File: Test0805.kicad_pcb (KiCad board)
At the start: 2 copper layers, 0 parts

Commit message: Position footprints.
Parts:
- added BT1: 9V, footprints:BatteryHolder_Keystone_968_1x9V, F.Cu at (134.6, 109.2)
- added D1: LED, LEDs:LED_0805, F.Cu at (136.5, 104.8)
- added D2: LED, LEDs:LED_0805, F.Cu at (136.5, 113.7)
- added D3: LED, LEDs:LED_0805, F.Cu at (145.4, 104.8)
- added D4: LED, LEDs:LED_0805, F.Cu at (145.4, 113.7)
- added R1: R, Resistors_SMD:R_0805, F.Cu at (141.0, 108.0)
- added R2: R, Resistors_SMD:R_0805, F.Cu at (141.0, 110.5)

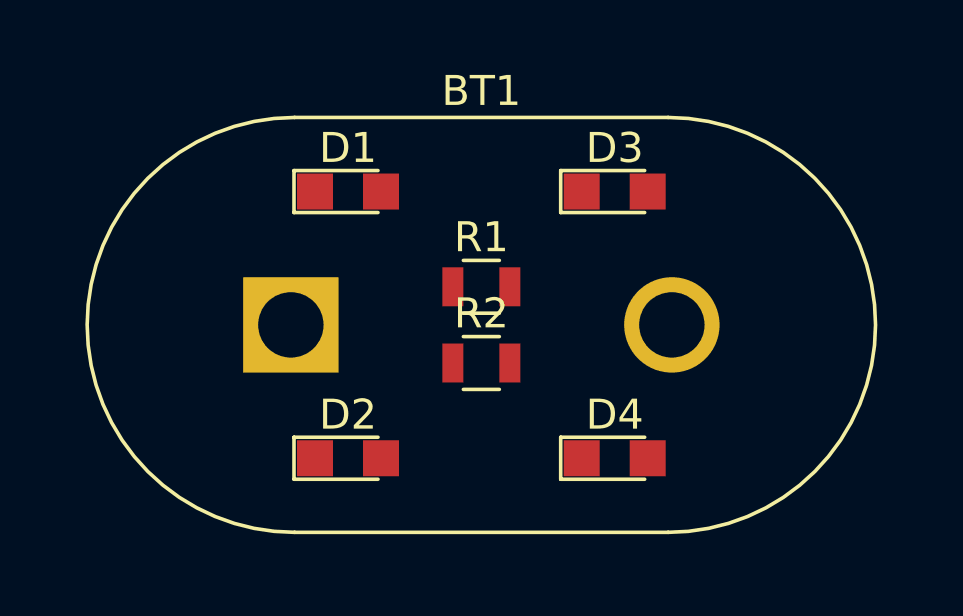
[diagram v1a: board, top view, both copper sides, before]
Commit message: Make references invisible.
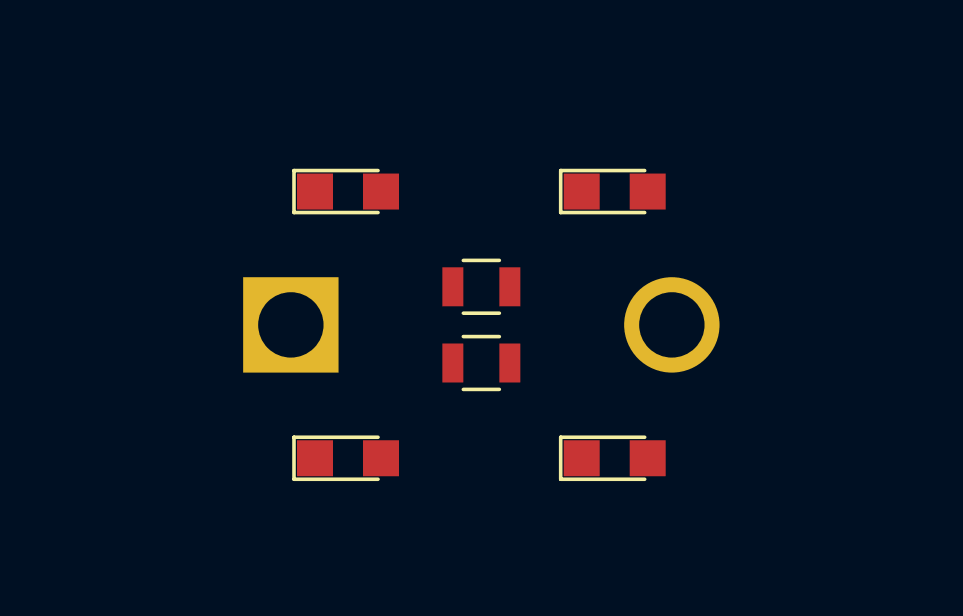
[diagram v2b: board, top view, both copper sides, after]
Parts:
- BT1: moved to B.Cu
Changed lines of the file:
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@@
     (46 B.CrtYd user)
     (47 F.CrtYd user)
-    (48 B.Fab user)
+    (48 B.Fab user hide)
     (49 F.Fab user hide)
   )
@@
     (add_net "Net-(D2-Pad2)")
   )
-  (module footprints:BatteryHolder_Keystone_968_1x9V (layer F.Cu)
+  (module footprints:BatteryHolder_Keystone_968_1x9V (layer B.Cu)
     (at 134.62 109.22)
     (descr "9V battery snap, http://www.keyelco.com/product-pdf.cfm?p=1072")
     (tags "9V battery snap")
-    (fp_text reference BT1 (at 6.35 -7.795) (layer F.SilkS)
-      (effects (font (size 1 1) (thickness 0.15)))
-    )
-    (fp_text value 9V (at 6.35 7.795) (layer F.Fab)
-      (effects (font (size 1 1) (thickness 0.15)))
-    )
-    (fp_arc (start 0.125 0) (end 0.125 6.795) (angle 180) (layer F.Fab) (width 0.1))
-    (fp_arc (start 12.575 0) (end 12.575 -6.795) (angle 180) (layer F.Fab) (width 0.1))
-    (fp_arc (start 0.125 0) (end 0.125 6.915) (angle 180) (layer F.SilkS) (width 0.12))
-    (fp_arc (start 12.575 0) (end 12.575 -6.915) (angle 180) (layer F.SilkS) (width 0.12))
-    (fp_line (start 0.125 -6.795) (end 12.575 -6.795) (layer F.Fab) (width 0.1))
-    (fp_line (start 0.125 6.795) (end 12.575 6.795) (layer F.Fab) (width 0.1))
-    (fp_line (start 0.125 -6.915) (end 12.575 -6.915) (layer F.SilkS) (width 0.12))
-    (fp_line (start 0.125 6.915) (end 12.575 6.915) (layer F.SilkS) (width 0.12))
-    (fp_line (start -7.17 -7.295) (end -7.17 7.295) (layer F.CrtYd) (width 0.05))
-    (fp_line (start -7.17 7.295) (end 19.87 7.295) (layer F.CrtYd) (width 0.05))
-    (fp_line (start 19.87 7.295) (end 19.87 -7.295) (layer F.CrtYd) (width 0.05))
-    (fp_line (start 19.87 -7.295) (end -7.17 -7.295) (layer F.CrtYd) (width 0.05))
-    (fp_text user %R (at 6.35 0) (layer F.Fab)
-      (effects (font (size 1 1) (thickness 0.15)))
+    (fp_text reference BT1 (at 6.35 7.795) (layer B.SilkS) hide
+      (effects (font (size 1 1) (thickness 0.15)) (justify mirror))
+    )
+    (fp_text value 9V (at 6.35 -7.795) (layer B.Fab)
+      (effects (font (size 1 1) (thickness 0.15)) (justify mirror))
+    )
+    (fp_arc (start 0.125 0) (end 0.125 -6.795) (angle -180) (layer B.Fab) (width 0.1))
+    (fp_arc (start 12.575 0) (end 12.575 6.795) (angle -180) (layer B.Fab) (width 0.1))
+    (fp_arc (start 0.125 0) (end 0.125 -6.915) (angle -180) (layer B.SilkS) (width 0.12))
+    (fp_arc (start 12.575 0) (end 12.575 6.915) (angle -180) (layer B.SilkS) (width 0.12))
+    (fp_line (start 0.125 6.795) (end 12.575 6.795) (layer B.Fab) (width 0.1))
+    (fp_line (start 0.125 -6.795) (end 12.575 -6.795) (layer B.Fab) (width 0.1))
+    (fp_line (start 0.125 6.915) (end 12.575 6.915) (layer B.SilkS) (width 0.12))
+    (fp_line (start 0.125 -6.915) (end 12.575 -6.915) (layer B.SilkS) (width 0.12))
+    (fp_line (start -7.17 7.295) (end -7.17 -7.295) (layer B.CrtYd) (width 0.05))
+    (fp_line (start -7.17 -7.295) (end 19.87 -7.295) (layer B.CrtYd) (width 0.05))
+    (fp_line (start 19.87 -7.295) (end 19.87 7.295) (layer B.CrtYd) (width 0.05))
+    (fp_line (start 19.87 7.295) (end -7.17 7.295) (layer B.CrtYd) (width 0.05))
+    (fp_text user %R (at 6.35 0) (layer B.Fab)
+      (effects (font (size 1 1) (thickness 0.15)) (justify mirror))
     )
     (pad 1 thru_hole rect (at 0 0) (size 3.18 3.18) (drill 2.18) (layers *.Cu *.Mask)
@@
     (tags "LED led 0805 SMD smd SMT smt smdled SMDLED smtled SMTLED")
     (attr smd)
-    (fp_text reference D1 (at 0 -1.45) (layer F.SilkS)
+    (fp_text reference D1 (at 0 -1.45) (layer F.SilkS) hide
       (effects (font (size 1 1) (thickness 0.15)))
     )
@@
     (tags "LED led 0805 SMD smd SMT smt smdled SMDLED smtled SMTLED")
     (attr smd)
-    (fp_text reference D2 (at 0 -1.45) (layer F.SilkS)
+    (fp_text reference D2 (at 0 -1.45) (layer F.SilkS) hide
       (effects (font (size 1 1) (thickness 0.15)))
     )
@@
     (tags "LED led 0805 SMD smd SMT smt smdled SMDLED smtled SMTLED")
     (attr smd)
-    (fp_text reference D3 (at 0 -1.45) (layer F.SilkS)
+    (fp_text reference D3 (at 0 -1.45) (layer F.SilkS) hide
       (effects (font (size 1 1) (thickness 0.15)))
     )
@@
     (tags "LED led 0805 SMD smd SMT smt smdled SMDLED smtled SMTLED")
     (attr smd)
-    (fp_text reference D4 (at 0 -1.45) (layer F.SilkS)
+    (fp_text reference D4 (at 0 -1.45) (layer F.SilkS) hide
       (effects (font (size 1 1) (thickness 0.15)))
     )
@@
     (tags "resistor 0805")
     (attr smd)
-    (fp_text reference R1 (at 0 -1.65) (layer F.SilkS)
+    (fp_text reference R1 (at 0 -1.65) (layer F.SilkS) hide
       (effects (font (size 1 1) (thickness 0.15)))
     )
@@
     (tags "resistor 0805")
     (attr smd)
-    (fp_text reference R2 (at 0 -1.65) (layer F.SilkS)
-      (effects (font (size 1 1) (thickness 0.15)))
-    )
+    (fp_text reference R2 (at 0 -1.65) (layer F.SilkS) hide
+      (effects (font (size 1 1) (thickness 0.15)))
+    )

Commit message: Add board outline.
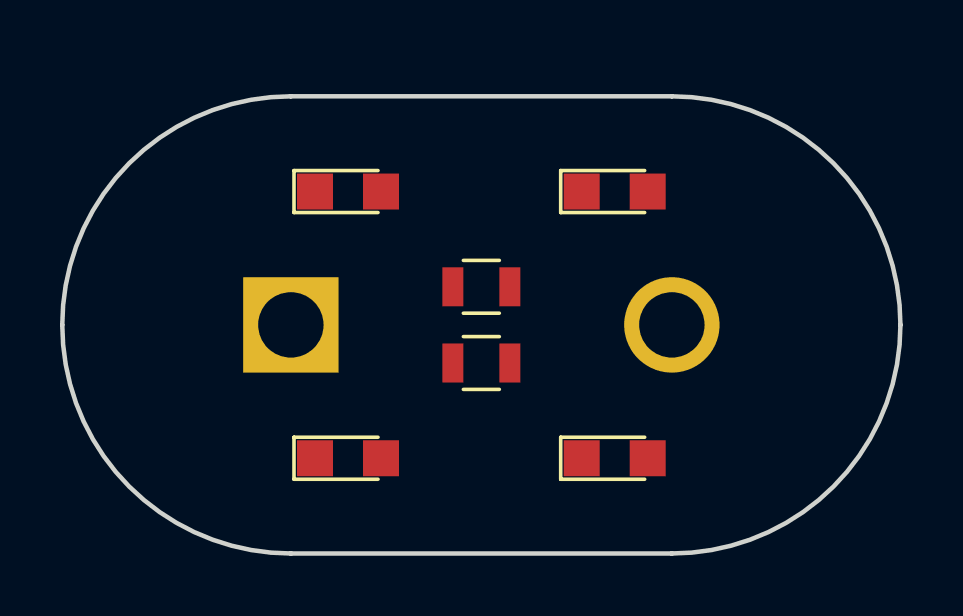
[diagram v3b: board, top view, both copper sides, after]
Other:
- board outline added: 27.9 x 15.2 mm
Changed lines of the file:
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@@
     (area 0 0 0 0)
     (thickness 1.6)
-    (drawings 0)
+    (drawings 6)
     (tracks 0)
     (zones 0)
@@
     )
   )
+  (gr_arc (start 147.32 109.22) (end 147.32 101.6) (angle 90) (layer Edge.Cuts) (width 0.15))
+  (gr_arc (start 147.32 109.22) (end 154.94 109.22) (angle 90) (layer Edge.Cuts) (width 0.15))
+  (gr_arc (start 134.62 109.22) (end 134.62 116.84) (angle 90) (layer Edge.Cuts) (width 0.15))
+  (gr_arc (start 134.62 109.22) (end 127 109.22) (angle 90) (layer Edge.Cuts) (width 0.15))
+  (gr_line (start 134.62 116.84) (end 147.32 116.84) (angle 90) (layer Edge.Cuts) (width 0.15))
+  (gr_line (start 134.62 101.6) (end 147.32 101.6) (angle 90) (layer Edge.Cuts) (width 0.15))
 )

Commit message: Add ground zones.
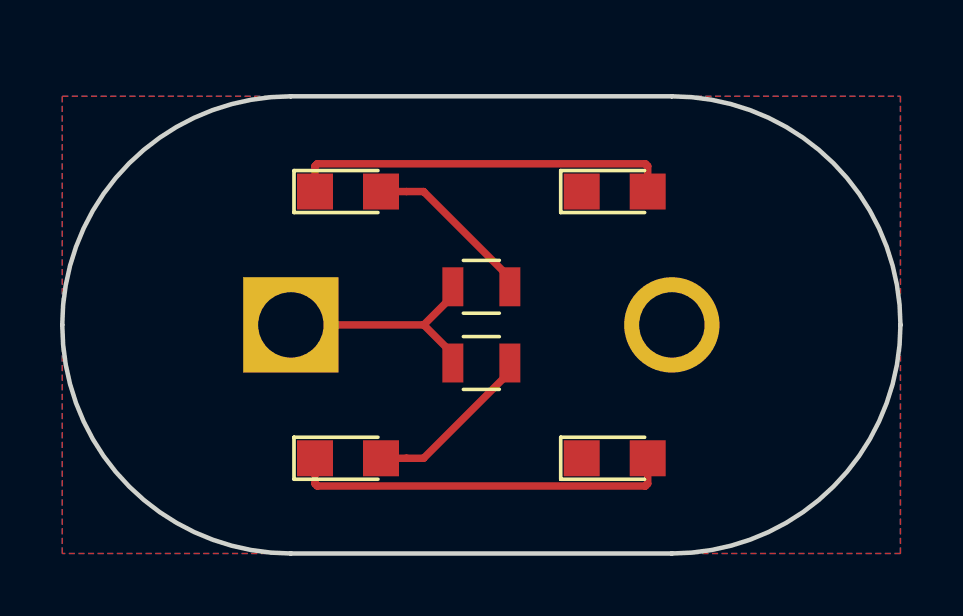
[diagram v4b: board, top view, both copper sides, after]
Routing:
- net Net-(D1-Pad1): track 0.00 -> 12.9 mm
- net Net-(D2-Pad1): track 0.00 -> 12.9 mm
- net Net-(BT1-Pad1): track 0.00 -> 7.77 mm
- net Net-(D2-Pad2): track 0.00 -> 5.79 mm
- net Net-(D1-Pad2): track 0.00 -> 5.79 mm
- added copper zone on B.Cu, net GND
- added copper zone on F.Cu, net GND
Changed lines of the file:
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@@
   (general
     (links 8)
-    (no_connects 8)
+    (no_connects 2)
     (area 0 0 0 0)
     (thickness 1.6)
     (drawings 6)
-    (tracks 0)
+    (tracks 23)
     (zones 0)
     (modules 7)
@@
     (44 Edge.Cuts user)
     (45 Margin user)
-    (46 B.CrtYd user)
+    (46 B.CrtYd user hide)
     (47 F.CrtYd user)
     (48 B.Fab user hide)
@@
     (last_trace_width 0.25)
     (trace_clearance 0.2)
-    (zone_clearance 0.508)
+    (zone_clearance 0.3048)
     (zone_45_only no)
     (trace_min 0.2)
@@
   (gr_line (start 134.62 116.84) (end 147.32 116.84) (angle 90) (layer Edge.Cuts) (width 0.15))
   (gr_line (start 134.62 101.6) (end 147.32 101.6) (angle 90) (layer Edge.Cuts) (width 0.15))
+  (segment (start 139.05 109.22) (end 140.02 110.19) (width 0.25) (layer F.Cu) (net 1))
+  (segment (start 140.02 110.19) (end 140.02 110.49) (width 0.25) (layer F.Cu) (net 1))
+  (segment (start 134.62 109.22) (end 139.05 109.22) (width 0.25) (layer F.Cu) (net 1))
+  (segment (start 139.05 109.22) (end 140.02 108.25) (width 0.25) (layer F.Cu) (net 1))
+  (segment (start 140.02 108.25) (end 140.02 107.95) (width 0.25) (layer F.Cu) (net 1))
+  (segment (start 141.92 107.95) (end 141.92 107.65) (width 0.25) (layer F.Cu) (net 3))
+  (segment (start 141.92 107.65) (end 139.045 104.775) (width 0.25) (layer F.Cu) (net 3))
+  (segment (start 139.045 104.775) (end 138.475 104.775) (width 0.25) (layer F.Cu) (net 3))
+  (segment (start 138.475 104.775) (end 137.625 104.775) (width 0.25) (layer F.Cu) (net 3))
+  (segment (start 135.425 104.775) (end 135.425 103.925) (width 0.25) (layer F.Cu) (net 4))
+  (segment (start 135.425 103.925) (end 135.500001 103.849999) (width 0.25) (layer F.Cu) (net 4))
+  (segment (start 135.500001 103.849999) (end 146.439999 103.849999) (width 0.25) (layer F.Cu) (net 4))
+  (segment (start 146.439999 103.849999) (end 146.515 103.925) (width 0.25) (layer F.Cu) (net 4))
+  (segment (start 146.515 103.925) (end 146.515 104.775) (width 0.25) (layer F.Cu) (net 4))
+  (segment (start 141.92 110.49) (end 141.92 110.79) (width 0.25) (layer F.Cu) (net 5))
+  (segment (start 141.92 110.79) (end 139.045 113.665) (width 0.25) (layer F.Cu) (net 5))
+  (segment (start 139.045 113.665) (end 138.475 113.665) (width 0.25) (layer F.Cu) (net 5))
+  (segment (start 138.475 113.665) (end 137.625 113.665) (width 0.25) (layer F.Cu) (net 5))
+  (segment (start 135.425 113.665) (end 135.425 114.515) (width 0.25) (layer F.Cu) (net 6))
+  (segment (start 135.425 114.515) (end 135.500001 114.590001) (width 0.25) (layer F.Cu) (net 6))
+  (segment (start 135.500001 114.590001) (end 146.439999 114.590001) (width 0.25) (layer F.Cu) (net 6))
+  (segment (start 146.439999 114.590001) (end 146.515 114.515) (width 0.25) (layer F.Cu) (net 6))
+  (segment (start 146.515 114.515) (end 146.515 113.665) (width 0.25) (layer F.Cu) (net 6))
+  (zone (net 2) (net_name GND) (layer F.Cu) (hatch edge 0.508)
+    (connect_pads (clearance 0.3048))
+    (min_thickness 0.254)
+    (fill (arc_segments 16) (thermal_gap 0.508) (thermal_bridge_width 0.508))
+    (polygon
+      (pts
+        (xy 154.94 116.84) (xy 127 116.84) (xy 127 101.6) (xy 154.94 101.6)
+      )
+    )
+  )
+  (zone (net 2) (net_name GND) (layer B.Cu) (hatch edge 0.508)
+    (connect_pads (clearance 0.3048))
+    (min_thickness 0.254)
+    (fill (arc_segments 16) (thermal_gap 0.508) (thermal_bridge_width 0.508))
+    (polygon
+      (pts
+        (xy 154.94 116.84) (xy 127 116.84) (xy 127 101.6) (xy 154.94 101.6)
+      )
+    )
+  )
 )
